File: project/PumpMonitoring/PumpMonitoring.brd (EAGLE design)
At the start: 160 x 100 mm, 28 parts, among them CN1 NC6-P108-02, Q1 BSS138, Q2 BSS84, Q3 BSS138, Q4 BSS138, Q5 BSS138, T1 IRLML2246, T2 IRLML2246, U1 FSS-71034-10x2,FSS-72034-05x1

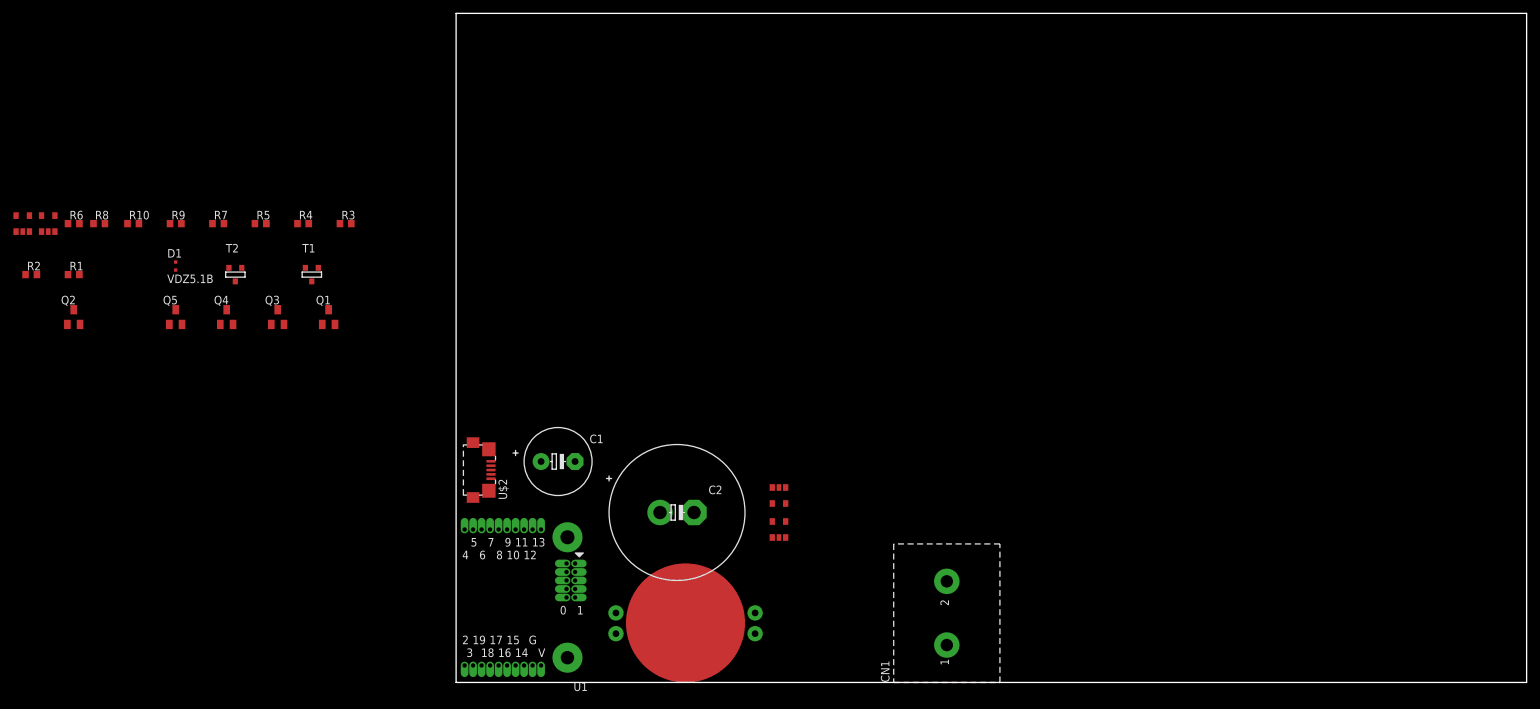
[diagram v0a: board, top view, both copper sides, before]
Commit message: update pump  monitoring.
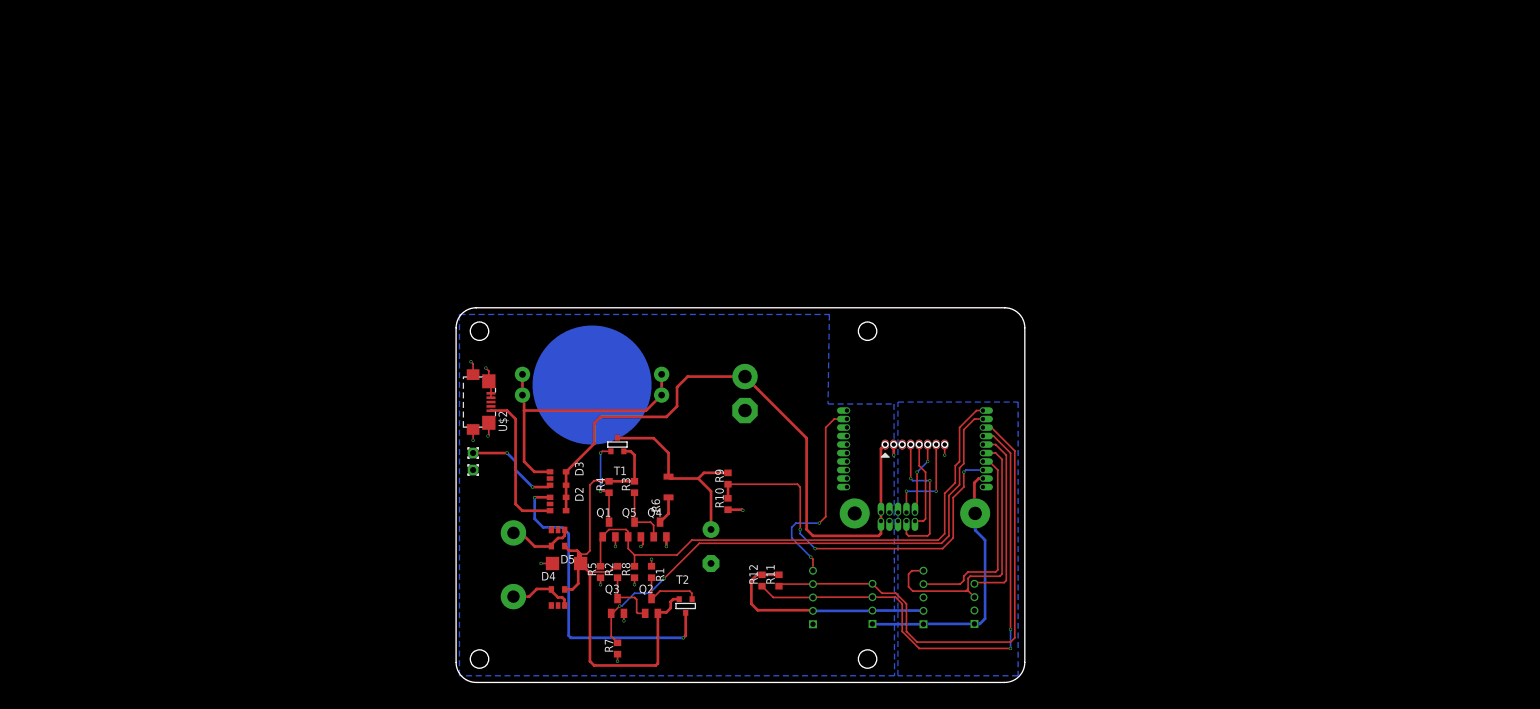
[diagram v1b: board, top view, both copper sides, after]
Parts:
- removed D8, D9: RRE04EA4D, rohm:TSMD5
- added CN2, CN7: (no value), jst-ph:B5B-PH-K-S
- added CN3, CN6: (no value), jst-ph:B4B-PH-K-S
- added D4, D5: RRE04EA4D, rohm2:TSMD5
- added PAD1, PAD2: (no value), wirepad:1,6/0,9
- added R11, R12: 1K, resistor:R0603
- added U$1: XB-1-X, lz-shield:XB-1-X
- D1: value VDZ5.1B -> PTZ6.2B; device rohm:VMD2 -> rohm2:DO214AC
- D2, D3: device rohm:TSMD5 -> rohm2:TSMD5
- R6: value 1k -> 10; device resistor:R0603 -> rohm2:EZP
- moved R10 98.3 mm to (40.6, 26.7), turned to 90 degrees
- moved R2 98.3 mm to (24.1, 16.5), turned to 90 degrees
- moved R6 97.2 mm to (31.8, 29.2), turned to 90 degrees
- moved R1 97.1 mm to (29.2, 16.5), turned to 270 degrees
- moved Q2 96.6 mm to (29.2, 11.4)
- moved R8 95.5 mm to (26.7, 16.5), turned to 90 degrees
- moved R9 90.9 mm to (40.6, 30.5), turned to 90 degrees
- moved R7 87.2 mm to (24.1, 5.08), turned to 90 degrees
- moved T2 83.6 mm to (34.3, 11.4)
- moved Q5 75.6 mm to (26.7, 22.9)
- moved D1 73.4 mm to (16.5, 17.8)
- moved R5 72.7 mm to (21.6, 16.5), turned to 90 degrees
- moved Q4 72.1 mm to (30.5, 22.9)
- moved CN1 70.5 mm to (16.5, 27.9), flipped to the bottom, turned to 270 degrees
- moved Q3 66.7 mm to (24.1, 11.4)
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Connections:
- removed net A4: U1.18
- removed net A5: U1.19
- removed net VCC5V: C2.+, D2.4, D2.5, D3.4, D3.5, U1.VCC5V_0, U1.VCC5V_1
- new net +3V3: CN2.2, CN3.2, CN6.2, CN7.2, R11.2, R12.2, U$1.8_1, U1.VCC3V_0, U1.VCC3V_1
- new net +5V: C2.+, D2.4, D2.5, D3.4, D3.5, U$1.1_1, U1.VCC5V_0, U1.VCC5V_1
- new net 0: U$1.6_1, U1.0
- new net 1: U$1.5_1, U1.1
- new net N$3: D3.3, PAD1.1
- new net SCL: CN2.4, CN6.4, R11.1, U1.19
- new net SDA: CN2.3, CN6.3, R12.1, U1.18
- net 5: now also CN2.5
- net A1: now also CN7.4
- net A2: now also CN3.3, CN7.5
- net A3: now also CN3.4
- net GND: now also CN2.1, CN3.1, CN6.1, CN7.1, D4.1, D5.3, PAD2.1, U$1.2_1; no longer D8.1, D9.1
- net I+: now also D4.3, D4.5; no longer D9.3, D9.5
- net I-: now also D5.1, D5.4; no longer D8.3, D8.5
- net IOUT: now also D4.4, D5.5; no longer D8.4, D9.4
- net TEST0: now also U$1.7_1
- net TEST1N: now also U$1.4_1
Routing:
- net +5V: track 0.00 -> 93.8 mm
- net 2: track 0.00 -> 83.6 mm
- net 3: track 0.00 -> 80.4 mm, vias 0 -> 2
- net IOUT: track 0.00 -> 78.2 mm
- net SDA: track 0.00 -> 77.9 mm, vias 0 -> 2
- net SCL: track 0.00 -> 75.8 mm
- net GND: track 0.00 -> 65.5 mm, vias 0 -> 15
- net A0: track 0.00 -> 58.0 mm, vias 0 -> 3
- net IOUT2: track 0.00 -> 47.9 mm, vias 0 -> 2
- net A2: track 0.00 -> 42.9 mm
- net N$2: track 0.00 -> 42.3 mm
- net +3V3: track 0.00 -> 35.8 mm, vias 0 -> 1
- net 5: track 0.00 -> 30.6 mm, vias 0 -> 2
- net A1: track 0.00 -> 30.0 mm
- net N$10: track 0.00 -> 29.9 mm
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- added copper zone on layer 16, net +3V3
- added copper zone on layer 16, net GND
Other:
- board size 160 x 100 mm -> 85 x 56 mm
- board text added: "A0"
- board text added: "ANALOG"
- board text added: "I2C"
- board text added: "MOTION"
- board text added: "SOUND"

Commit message: modify schematic of sound detect module.
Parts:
- removed PAD1, PAD2: (no value), wirepad:1,6/0,9
- added CN4: (no value), jst-ph:B2B-PH-K-S
- moved D1 2.01 mm to (14.6, 17.1)
- moved U$2 1.27 mm to (2.54, 43.2)
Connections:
- net GND: now also CN4.2; no longer PAD2.1
- net N$3: now also CN4.1; no longer PAD1.1
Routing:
- net N$2: track 42.3 -> 38.8 mm
- net VEXT: track 22.5 -> 23.7 mm
- net GND: track 65.5 -> 65.8 mm, vias 15 -> 17
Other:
- board text added: "A2"
- board text added: "LAPIS Semiconductor Co.,Ltd."
- board text added: "Lazurite mini CT Sensor Shiled"
- board text removed: "A0"
- board text removed: "ANALOG"
